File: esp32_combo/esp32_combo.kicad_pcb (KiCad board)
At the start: 2 copper layers, 90 x 43 mm, 35 parts, among them J1 TERM BLK 3.5MM 2P SIDE, J2 TERM BLK 3.5MM 6P SIDE, J3 TERM BLK 3.5MM 6P SIDE, J4 TERM BLK 3.5MM 3P SIDE, J5 TERM BLK 3.5MM 3P SIDE, J6 HDR SKT 5PIN VERT 2.54MM, J7 HDR SKT 6PIN VERT 2.54MM, J8 SKT 2x6PIN VERT 2.54MM, J9 HDR SKT 8PIN VERT 2.54MM, Q1 AS2302, SW1 SS12D10, U1 TB6612FNG Module, U2 ESP32 DEV KIT Module 30-pin, U3 LM2596 Module

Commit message: Combo routed
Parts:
- J7: value HDR SKT 6PIN VERT 2.54MM -> HDR SKT 5PIN VERT 2.54MM; footprint Connector_PinSocket_2.54mm:PinSocket_1x06_P2.54mm_Vertical -> Connector_PinSocket_2.54mm:PinSocket_1x05_P2.54mm_Vertical
- J8: value SKT 2x6PIN VERT 2.54MM -> SKT 2x5PIN VERT 2.54MM; footprint Connector_PinSocket_2.54mm:PinSocket_2x06_P2.54mm_Vertical -> Connector_PinSocket_2.54mm:PinSocket_2x05_P2.54mm_Vertical
- J9: value HDR SKT 8PIN VERT 2.54MM -> HDR SKT 7PIN VERT 2.54MM; footprint Connector_PinSocket_2.54mm:PinSocket_1x08_P2.54mm_Vertical -> Connector_PinSocket_2.54mm:PinSocket_1x07_P2.54mm_Vertical
- moved J4 31.0 mm to (82.8, 33.8)
- moved J7 28.6 mm to (84.7, 59.2), turned to 0 degrees
- moved D1 21.2 mm to (51.7, 43.8), turned to -90 degrees
- moved H2 9.88 mm to (117.7, 69.7)
- moved J8 4.14 mm to (92.8, 59.2)
- moved G*** 3.63 mm to (57.7, 51.9)
- moved J5 2.67 mm to (101.7, 69.1)
- moved U1 2.67 mm to (105.2, 62.3)
- moved R10 1.91 mm to (55.3, 43.2)
- moved H3 1.73 mm to (82.2, 42.0)
- moved R3 1.51 mm to (58.1, 43.2)
- moved SW1 1.44 mm to (63.8, 33.4)
- moved D2 0.90 mm to (53.2, 35.3)
- moved F1 0.90 mm to (50.9, 35.2)
- moved J6 0.40 mm to (49.1, 69.6)
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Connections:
- J7 pad 2: +5V -> /GPIO27
- J7 pad 3: /GPIO27 -> /GPIO18
- J7 pad 4: /GPIO18 -> /GPIO5_BOOT_STRAP
- J7 pad 5: /GPIO5_BOOT_STRAP -> /GPIO4
- J8 pad 10: /I2C_SDA -> +5V
- J8 pad 3: GND -> /I2C_SCL
- J8 pad 4: GND -> /I2C_SCL
- J8 pad 5: +5V -> /I2C_SDA
- J8 pad 6: +5V -> /I2C_SDA
- J8 pad 7: /I2C_SCL -> /I2C_INT
- J8 pad 8: /I2C_SCL -> /I2C_INT
- J8 pad 9: /I2C_SDA -> +5V
- J9 pad 2: GND -> +5V
- J9 pad 3: +5V -> /LDS_PWM
- J9 pad 4: /MOT -> Net-(J9-Pin_4)
- J9 pad 5: /LDS_PWM -> /LDS_RX
- J9 pad 6: /LDS_EN -> /MOT
- J9 pad 7: Net-(J9-Pin_7) -> /LDS_EN
- R11 pad 2: Net-(J9-Pin_7) -> Net-(J9-Pin_4)
- U2 pad 23: /CW_RIGHT -> /PWM_RIGHT
- U2 pad 28: /PWM_RIGHT -> /CW_RIGHT
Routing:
- net +5V: track 245.2 -> 198.0 mm, vias 3 -> 2
- net /CW_LEFT: track 45.1 -> 78.9 mm
- net Vdrive: track 139.4 -> 105.9 mm
- net Net-(J9-Pin_7): track 32.0 -> 0.00 mm
- net Net-(J9-Pin_4): track 0.00 -> 25.0 mm
- net /GPIO5_BOOT_STRAP: track 49.1 -> 27.0 mm, vias 2 -> 0
- net /PWM_RIGHT: track 83.5 -> 61.5 mm
- net /GPIO4: track 56.0 -> 35.0 mm, vias 2 -> 0
- net Net-(D1-K): track 31.6 -> 12.2 mm
- net /GPIO18: track 44.7 -> 26.7 mm, vias 2 -> 0
- net /GPIO27: track 27.8 -> 43.6 mm
- net /CW_RIGHT: track 72.8 -> 86.3 mm
- net +3V3: track 75.0 -> 63.7 mm
- net /GPIO12_OUT_STRAP: track 60.4 -> 69.3 mm
- net /LDS_EN: track 15.9 -> 24.2 mm
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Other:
- board text added: "A01"
- board text added: "A02"
- board text added: "AI1"
- board text added: "AI2"
- board text added: "B01"
- board text added: "B02"
- board text added: "BI1"
- board text added: "BI2"
- board text added: "GPIO"
- board text added: "MakersCOMBO 1.0"
- board text added: "PWA"
- board text added: "PWB"
- board text added: "SBY"
- board text added: "VCC"

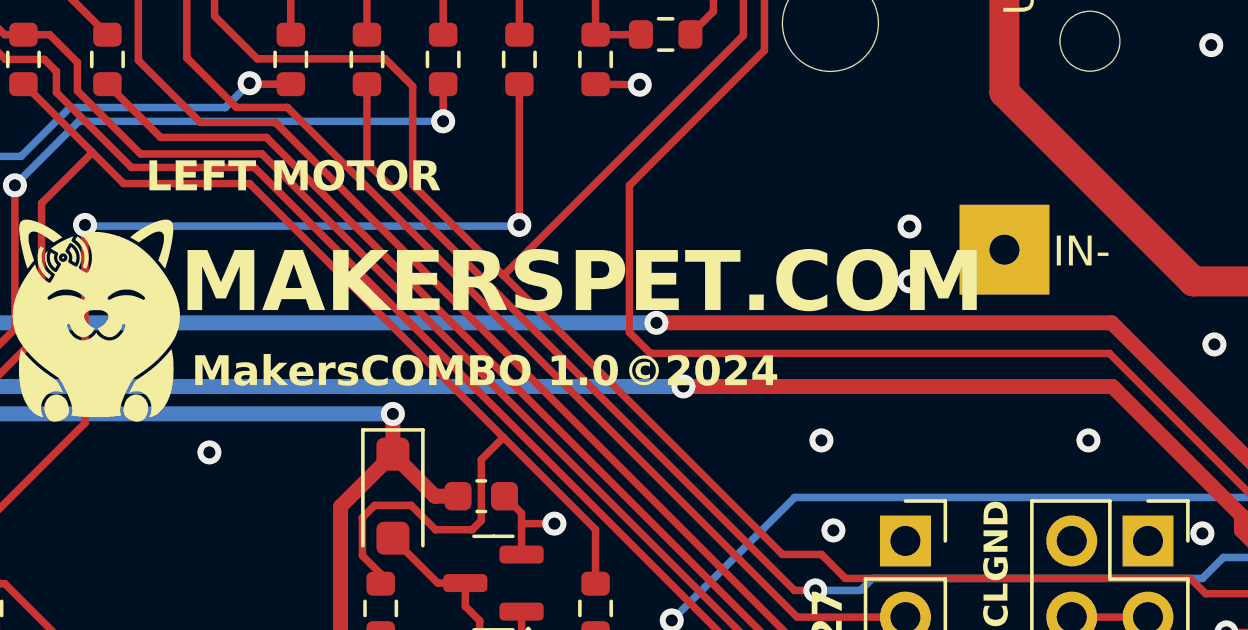
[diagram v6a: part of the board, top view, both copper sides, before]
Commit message: esp32_combo, pico_breakout_head
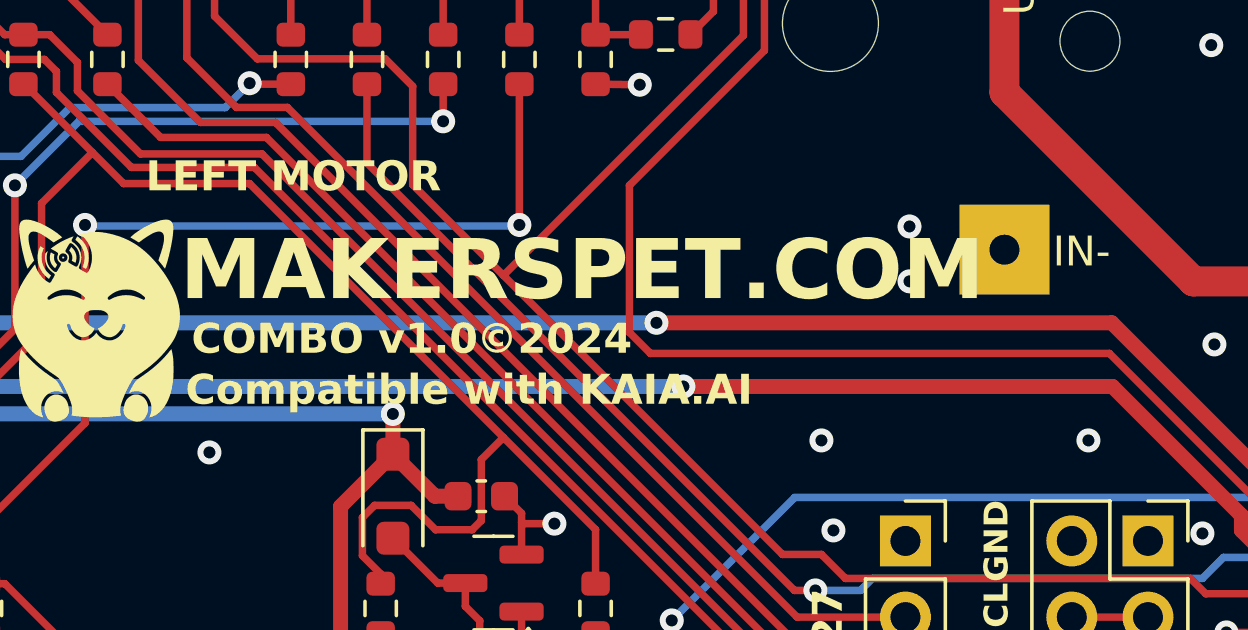
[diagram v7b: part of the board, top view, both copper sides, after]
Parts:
- moved G*** 40.5 mm to (81.2, 51.8)
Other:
- board text added: "Battery voltage 9..12V if using TB6612FNG 9..24V with TB6612FNG removed Max current 3A"
- board text added: "COMBO v1.0"
- board text added: "Compatible with KAIA.AI"
- board text removed: "MakersCOMBO 1.0"
- board text removed: "MakersCOMBO v1.0"
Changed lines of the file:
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@@
 			(usegerberattributes yes)
 			(usegerberadvancedattributes yes)
-			(creategerberjobfile yes)
+			(creategerberjobfile no)
 			(dashed_line_dash_ratio 12.000000)
 			(dashed_line_gap_ratio 3.000000)
@@
 	(footprint "Makerspet:Maker's Pet Logo 7mm"
 		(layer "B.Cu")
-		(at 119.9896 40.2082 180)
+		(at 81.188602 51.8 180)
 		(property "Reference" "G***"
-			(at 0 0 0)
+			(at 0 0 180)
 			(layer "B.SilkS")
 			(hide yes)
@@
 		)
 		(property "Value" "LOGO"
-			(at 0.75 0 0)
+			(at 0.75 0 180)
 			(layer "B.SilkS")
 			(hide yes)
@@
 		)
 		(property "Footprint" ""
-			(at 0 0 180)
+			(at 0 0 0)
 			(unlocked yes)
-			(layer "F.Fab")
+			(layer "B.Fab")
 			(hide yes)
 			(effects
@@
 					(size 1.27 1.27)
 				)
+				(justify mirror)
 			)
 		)
 		(property "Datasheet" ""
-			(at 0 0 180)
+			(at 0 0 0)
 			(unlocked yes)
-			(layer "F.Fab")
+			(layer "B.Fab")
 			(hide yes)
 			(effects
@@
 					(size 1.27 1.27)
 				)
+				(justify mirror)
 			)
 		)
 		(property "Description" ""
-			(at 0 0 180)
+			(at 0 0 0)
 			(unlocked yes)
-			(layer "F.Fab")
+			(layer "B.Fab")
 			(hide yes)
 			(effects
@@
 					(size 1.27 1.27)
 				)
+				(justify mirror)
 			)
 		)
@@
 		(layer "Edge.Cuts")
 	)
-	(gr_text "MakersCOMBO v1.0"
-		(at 116.586 41.91 0)
+	(gr_text "MAKERSPET.COM"
+		(at 78.394602 51.2984 -0)
+		(layer "B.SilkS")
+		(effects
+			(font
+				(size 2 2)
+				(thickness 0.4)
+				(bold yes)
+			)
+			(justify left bottom mirror)
+		)
+	)
+	(gr_text "Compatible with KAIA.AI"
+		(at 78.213602 54.7 -0)
+		(layer "B.SilkS")
+		(effects
+			(font
+				(size 1 1)
+				(thickness 0.25)
+				(bold yes)
+			)
+			(justify left bottom mirror)
+		)
+	)
+	(gr_text "COMBO v1.0"
+		(at 78.013602 53 -0)
 		(layer "B.SilkS" knockout)
 		(effects
 			(font
 				(size 1 1)
-				(thickness 0.2)
+				(thickness 0.25)
 				(bold yes)
 			)
@@
 		)
 	)
-	(gr_text "©2024"
-		(at 102 41.91 0)
+	(gr_text "Battery voltage\n9..12V if using TB6612FNG\n9..24V with TB6612FNG removed\nMax current 3A"
+		(at 119 44.4 0)
 		(layer "B.SilkS")
 		(effects
@@
 		)
 	)
-	(gr_text "MAKERSPET.COM"
-		(at 116.9416 39.8526 0)
+	(gr_text "©2024"
+		(at 68.513602 53 -0)
 		(layer "B.SilkS")
 		(effects
 			(font
-				(size 2 2)
-				(thickness 0.3)
+				(size 1 1)
+				(thickness 0.25)
+				(bold yes)
 			)
 			(justify left bottom mirror)
@@
 	)
 	(gr_text "©2024"
-		(at 75.3 54.1828 0)
+		(at 70.4 53.1 0)
 		(layer "F.SilkS")
 		(effects
@@
 		)
 	)
-	(gr_text "MakersCOMBO 1.0"
-		(at 60.9 54.1828 0)
+	(gr_text "COMBO v1.0"
+		(at 60.9 53.1 0)
 		(layer "F.SilkS" knockout)
 		(effects
@@
 	)
 	(gr_text "MAKERSPET.COM"
-		(at 60.519 51.7984 0)
+		(at 60.519 51.3984 0)
 		(layer "F.SilkS")
 		(effects
@@
 				(bold yes)
 			)
+			(justify left bottom)
+		)
+	)
+	(gr_text "Compatible with KAIA.AI"
+		(at 60.7 54.8 0)
+		(layer "F.SilkS")
+		(effects
+			(font
+				(size 1 1)
+				(thickness 0.25)
+				(bold yes)
+			)
